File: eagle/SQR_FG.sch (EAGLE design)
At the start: 24 parts, among them IC1 MEGA328P, IC2 NJM7032, Q1 16MHz, SW1 EC12E_SW

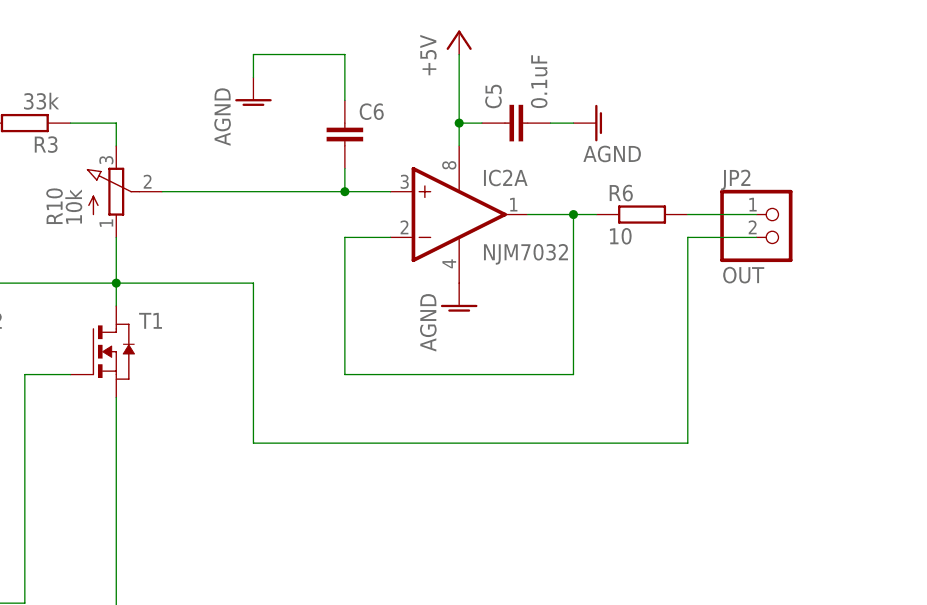
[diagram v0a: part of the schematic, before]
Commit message: eagle: Add Bypass Connector
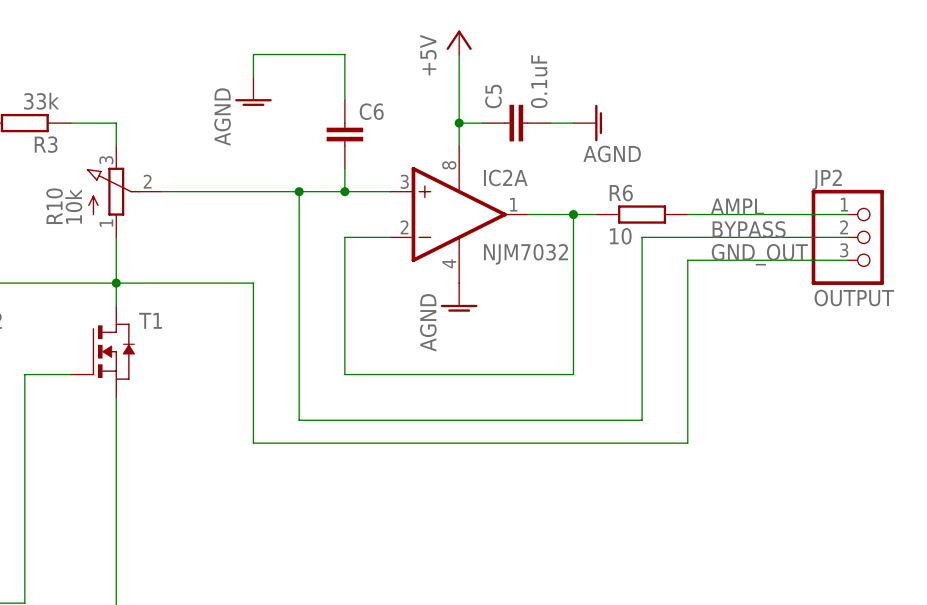
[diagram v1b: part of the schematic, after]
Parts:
- JP2: value OUT -> OUTPUT; device pinhead:PINHD-1X2 -> pinhead:PINHD-1X3
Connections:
- net N$11 renamed AMPL
- removed net N$15: C6.2, IC2A.+IN
- removed net N$6: JP2.2, R10.A, T1.D, T2.D
- new net BYPASS: C6.2, IC2A.+IN, JP2.2
- new net GND_OUT: JP2.3, R10.A, T1.D, T2.D
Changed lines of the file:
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@@
 <setting verticaltext="up"/>
 </settings>
-<grid distance="0.1" unitdist="inch" unit="inch" style="lines" multiple="1" display="no" altdistance="0.01" altunitdist="inch" altunit="inch"/>
+<grid distance="0.1" unitdist="inch" unit="inch" style="dots" multiple="1" display="yes" altdistance="0.01" altunitdist="inch" altunit="inch"/>
 <layers>
 <layer number="1" name="Top" color="4" fill="1" visible="no" active="no"/>
@@
 <part name="T2" library="zetex" deviceset="NMOSE3L" device=""/>
 <part name="C5" library="rcl" deviceset="C-EU" device="025-024X044" value="0.1uF"/>
-<part name="JP2" library="pinhead" deviceset="PINHD-1X2" device="" value="OUT"/>
 <part name="R3" library="rcl" deviceset="R-EU_" device="0207/7" value="33k"/>
 <part name="C6" library="rcl" deviceset="C-EU" device="025-024X044"/>
@@
 <part name="C3" library="rcl" deviceset="CPOL-EU" device="E2.5-5" value="100uF"/>
 <part name="C7" library="rcl" deviceset="CPOL-EU" device="E2.5-5" value="100uF"/>
+<part name="JP2" library="pinhead" deviceset="PINHD-1X3" device="" value="OUTPUT"/>
 </parts>
 <sheets>
@@
 <instance part="T2" gate="A" x="165.1" y="78.74"/>
 <instance part="C5" gate="G$1" x="226.06" y="104.14" rot="R90"/>
-<instance part="JP2" gate="G$1" x="256.54" y="91.44"/>
 <instance part="R3" gate="G$1" x="172.72" y="104.14" rot="R180"/>
 <instance part="C6" gate="G$1" x="208.28" y="104.14"/>
@@
 <instance part="C3" gate="G$1" x="144.78" y="40.64"/>
 <instance part="C7" gate="G$1" x="144.78" y="22.86"/>
+<instance part="JP2" gate="A" x="266.7" y="91.44"/>
 </instances>
 <busses>
@@
 </segment>
 </net>
-<net name="N$11" class="0">
+<net name="AMPL" class="0">
 <segment>
 <pinref part="R6" gate="G$1" pin="2"/>
-<wire x1="246.38" y1="93.98" x2="254" y2="93.98" width="0.1524" layer="91"/>
-<pinref part="JP2" gate="G$1" pin="1"/>
+<wire x1="246.38" y1="93.98" x2="264.16" y2="93.98" width="0.1524" layer="91"/>
+<pinref part="JP2" gate="A" pin="1"/>
+<label x="248.92" y="93.98" size="1.778" layer="95"/>
 </segment>
 </net>
@@
 </segment>
 </net>
-<net name="N$6" class="0">
+<net name="GND_OUT" class="0">
 <segment>
 <pinref part="R10" gate="G$1" pin="A"/>
@@
 <wire x1="198.12" y1="86.36" x2="198.12" y2="68.58" width="0.1524" layer="91"/>
 <wire x1="198.12" y1="68.58" x2="246.38" y2="68.58" width="0.1524" layer="91"/>
-<wire x1="246.38" y1="68.58" x2="246.38" y2="91.44" width="0.1524" layer="91"/>
-<pinref part="JP2" gate="G$1" pin="2"/>
-<wire x1="254" y1="91.44" x2="246.38" y2="91.44" width="0.1524" layer="91"/>
+<wire x1="246.38" y1="68.58" x2="246.38" y2="88.9" width="0.1524" layer="91"/>
+<pinref part="JP2" gate="A" pin="3"/>
+<wire x1="264.16" y1="88.9" x2="246.38" y2="88.9" width="0.1524" layer="91"/>
+<label x="248.92" y="88.9" size="1.778" layer="95"/>
 </segment>
 </net>
@@
 </segment>
 </net>
-<net name="N$15" class="0">
-<segment>
-<wire x1="187.96" y1="96.52" x2="208.28" y2="96.52" width="0.1524" layer="91"/>
+<net name="BYPASS" class="0">
+<segment>
+<wire x1="187.96" y1="96.52" x2="203.2" y2="96.52" width="0.1524" layer="91"/>
 <pinref part="IC2" gate="A" pin="+IN"/>
 <pinref part="C6" gate="G$1" pin="2"/>
+<wire x1="203.2" y1="96.52" x2="208.28" y2="96.52" width="0.1524" layer="91"/>
 <wire x1="208.28" y1="96.52" x2="213.36" y2="96.52" width="0.1524" layer="91"/>
 <wire x1="208.28" y1="99.06" x2="208.28" y2="96.52" width="0.1524" layer="91"/>
 <junction x="208.28" y="96.52"/>
-</segment>
-</net>
+<pinref part="JP2" gate="A" pin="2"/>
+<wire x1="264.16" y1="91.44" x2="241.3" y2="91.44" width="0.1524" layer="91"/>
+<wire x1="241.3" y1="91.44" x2="241.3" y2="71.12" width="0.1524" layer="91"/>
+<wire x1="241.3" y1="71.12" x2="203.2" y2="71.12" width="0.1524" layer="91"/>
+<wire x1="203.2" y1="71.12" x2="203.2" y2="96.52" width="0.1524" layer="91"/>
+<junction x="203.2" y="96.52"/>
+<label x="248.92" y="91.44" size="1.778" layer="95"/>
+</segment>
+</net>

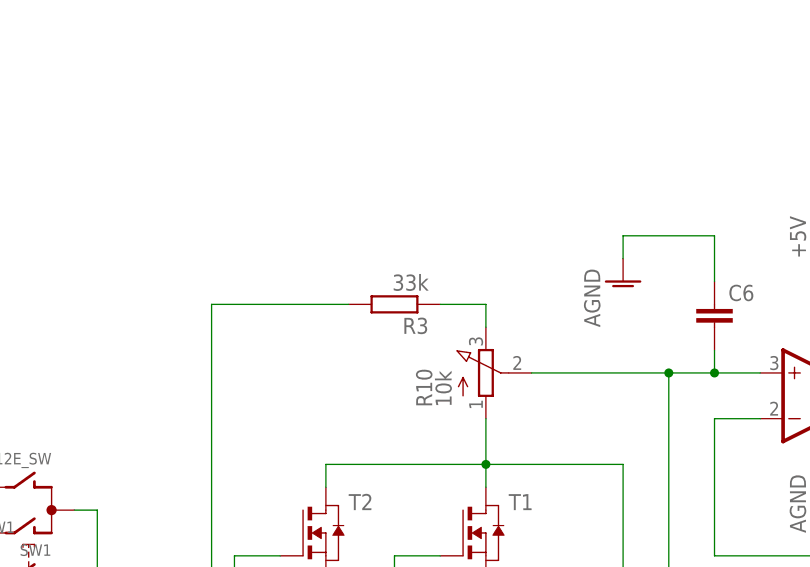
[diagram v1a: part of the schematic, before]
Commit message: Change eagle SQR_FG.sch R value
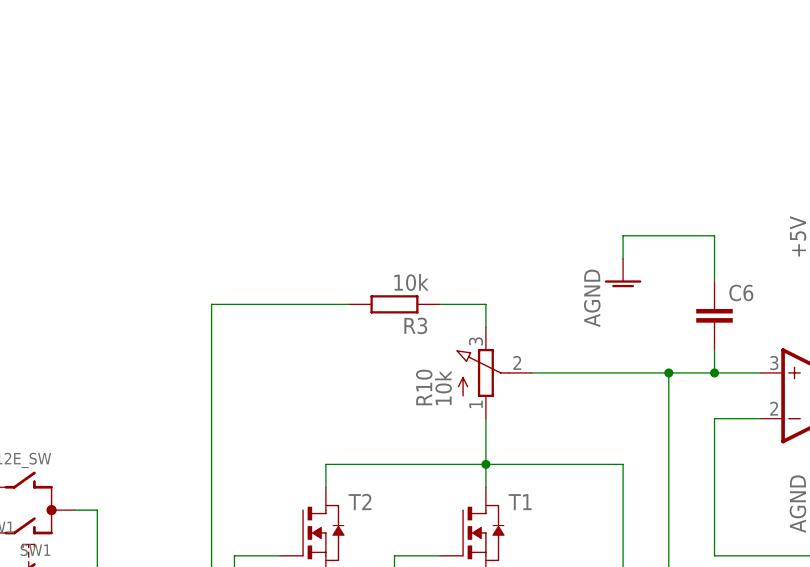
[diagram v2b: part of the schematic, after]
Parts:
- R3: value 33k -> 10k
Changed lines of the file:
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@@
 <part name="T2" library="zetex" deviceset="NMOSE3L" device=""/>
 <part name="C5" library="rcl" deviceset="C-EU" device="025-024X044" value="0.1uF"/>
-<part name="R3" library="rcl" deviceset="R-EU_" device="0207/7" value="33k"/>
+<part name="R3" library="rcl" deviceset="R-EU_" device="0207/7" value="10k"/>
 <part name="C6" library="rcl" deviceset="C-EU" device="025-024X044"/>
 <part name="AGND1" library="supply1" deviceset="AGND" device=""/>

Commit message: before editing SQR_FG.brd
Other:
- note added: "⇒別基板"
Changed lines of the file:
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@@
 <setting verticaltext="up"/>
 </settings>
-<grid distance="0.1" unitdist="inch" unit="inch" style="dots" multiple="1" display="yes" altdistance="0.01" altunitdist="inch" altunit="inch"/>
+<grid distance="0.1" unitdist="inch" unit="inch" style="lines" multiple="1" display="no" altdistance="0.01" altunitdist="inch" altunit="inch"/>
 <layers>
 <layer number="1" name="Top" color="4" fill="1" visible="no" active="no"/>
@@
 <wire x1="142.24" y1="88.9" x2="121.92" y2="88.9" width="0" layer="100" style="shortdash"/>
 <text x="132.08" y="91.44" size="1.778" layer="100">Rotary Encoder</text>
+<wire x1="205.74" y1="152.4" x2="190.5" y2="152.4" width="0.1524" layer="100"/>
+<wire x1="190.5" y1="152.4" x2="190.5" y2="2.54" width="0.1524" layer="100"/>
+<text x="198.12" y="139.7" size="6.4516" layer="100" font="fixed">⇒別基板</text>
 </plain>
 <instances>

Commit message: SQR_FG.brd SQR_FG board design editing.
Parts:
- removed R10: 10k, pot:3RP/1610N
- removed R2: 10k/B, pot:3RP/1610N
- removed SW1: EC12E_SW, switch-alps:EC12E_SW
- added JP3: (no value), pinhead:PINHD-1X3
- added JP4: Level Vol, pinhead:PINHD-1X3
- added JP5: (no value), pinhead:PINHD-1X4
- added JP6: SQR_OUT, pinhead:PINHD-1X2
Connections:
- new net N$4: JP4.2, JP6.1
- new net N$5: JP4.1, JP6.2, T1.D, T2.D
- net +5V: now also JP3.1; no longer R2.A
- net GND: now also JP3.3, JP5.4; no longer R2.E, SW1G$1.C, SW1G$2.1
- net GND_OUT: no longer R10.A, T1.D, T2.D
- net N$8: now also JP4.3; no longer R10.E
- net N$9: now also JP3.2; no longer R2.S
- net RE_A: now also JP5.1; no longer SW1G$1.B
- net RE_B: now also JP5.2; no longer SW1G$1.A
- net RE_SW: now also JP5.3; no longer SW1G$2.2
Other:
- moved on the sheet: R3
